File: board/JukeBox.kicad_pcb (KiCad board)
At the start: 2 copper layers, 78.5 x 80 mm, 44 parts, among them J1 USB_C_Receptacle_USB2.0, J2 Conn_01x02, J3 Conn_01x04, J4 Conn_01x03, SW1 SW_SPST, SW10 SW_SPST, SW11 SW_SPST, SW12 SW_SPST, SW2 SW_SPST, SW3 SW_SPST, SW4 SW_SPST, SW5 SW_SPST, SW6 SW_SPST, SW7 SW_SPST, SW8 SW_SPST, SW9 SW_SPST, U1 ATmega8U2-A, Y1 16MHz

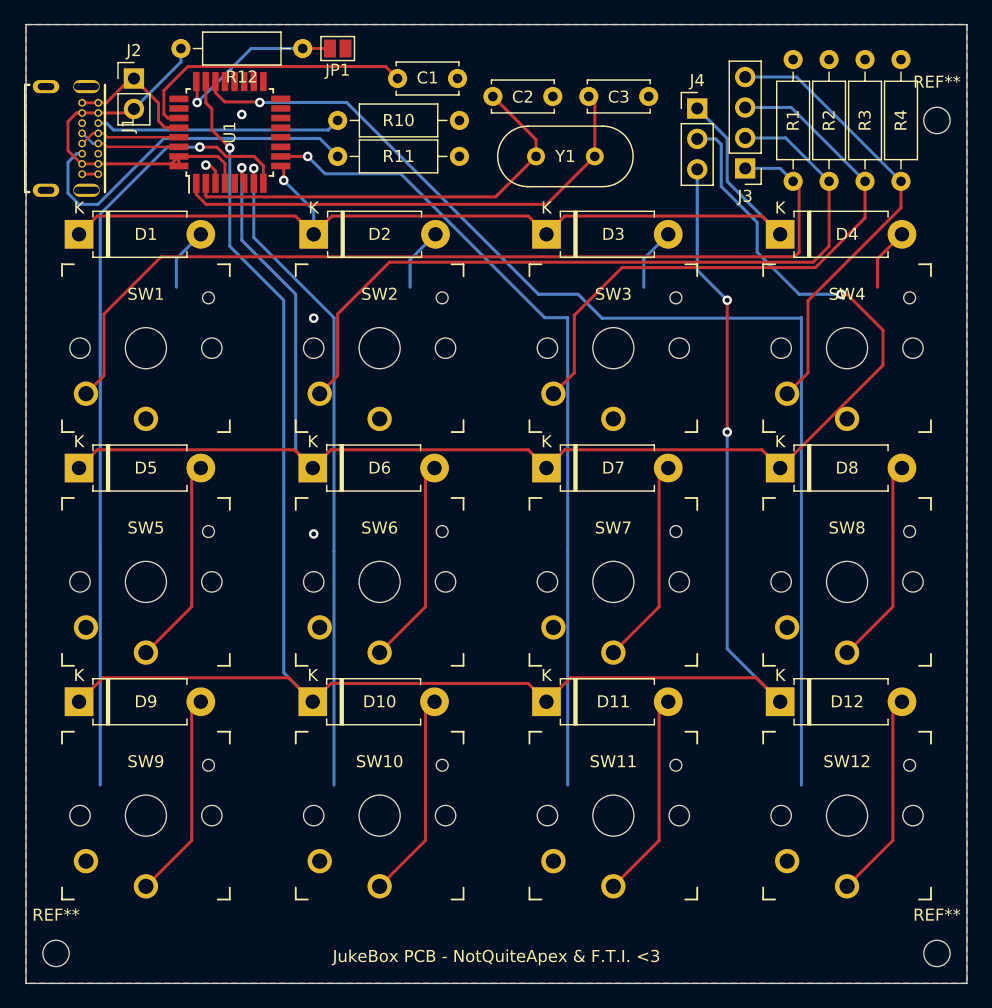
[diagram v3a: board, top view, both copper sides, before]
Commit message: update traces and usb c pads
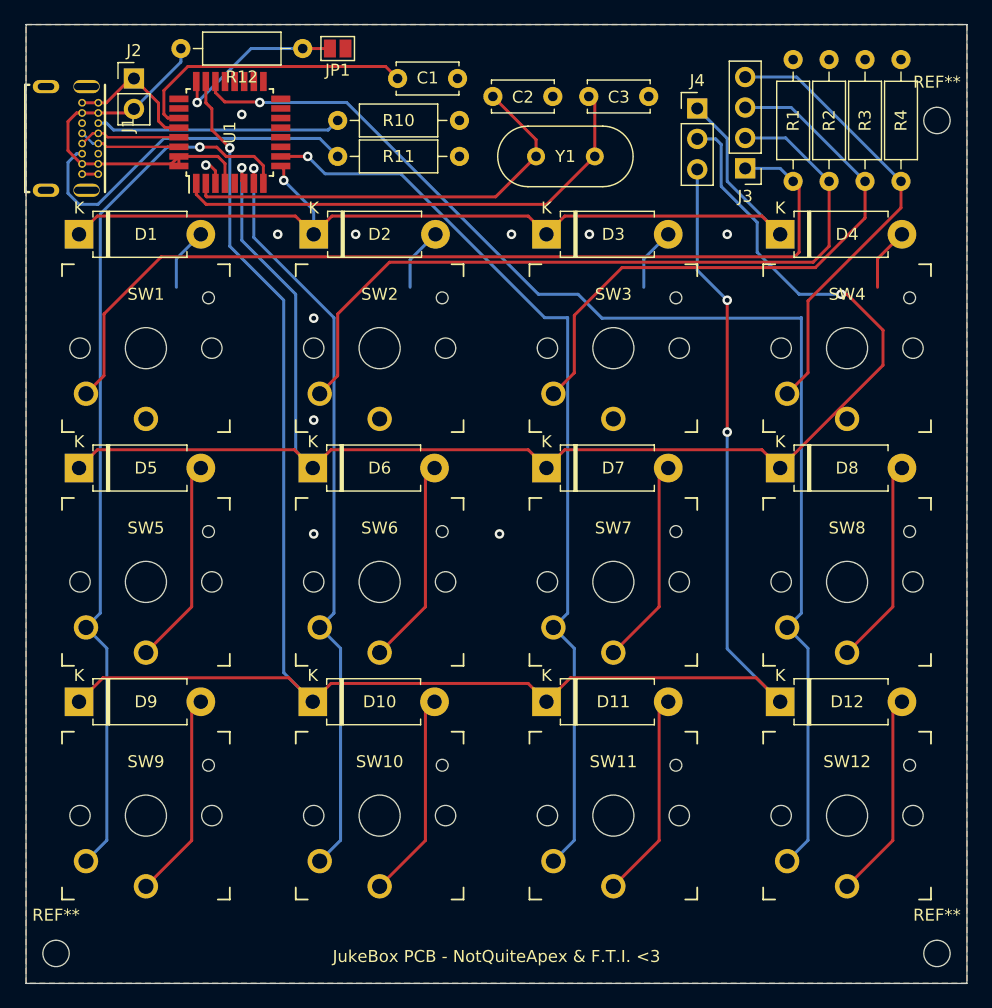
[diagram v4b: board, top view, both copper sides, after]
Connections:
- J1 pad P1: (no net) -> GND
- J1 pad P2: (no net) -> GND
- J1 pad P3: (no net) -> GND
- J1 pad P4: (no net) -> GND
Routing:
- net COL_4: track 134.9 -> 143.2 mm
- net COL_3: track 119.0 -> 127.3 mm
- net COL_1: track 143.7 -> 152.0 mm
- net COL_2: track 120.0 -> 128.3 mm
- net GND: vias 4 -> 11
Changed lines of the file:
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@@
     (pad "B12" thru_hole circle locked (at -2.975 -2.675 270) (size 0.65 0.65) (drill 0.4) (layers *.Cu *.Mask)
       (net 1 "GND") (pinfunction "GND") (pintype "passive"))
-    (pad "P1" thru_hole oval locked (at -4.325 -3.045 270) (size 1.108 2.216) (drill oval 0.6 2.1) (layers *.Cu *.Mask))
-    (pad "P2" thru_hole oval locked (at 4.325 -3.045 270) (size 1.108 2.216) (drill oval 0.6 2.1) (layers *.Cu *.Mask))
-    (pad "P3" thru_hole oval locked (at 4.325 0.335 270) (size 1.108 2.216) (drill oval 0.6 1.4) (layers *.Cu *.Mask))
-    (pad "P4" thru_hole oval locked (at -4.325 0.335 270) (size 1.108 2.216) (drill oval 0.6 1.4) (layers *.Cu *.Mask))
+    (pad "P1" thru_hole oval locked (at -4.325 -3.045 270) (size 1.108 2.216) (drill oval 0.6 2.1) (layers *.Cu *.Mask)
+      (net 1 "GND"))
+    (pad "P2" thru_hole oval locked (at 4.325 -3.045 270) (size 1.108 2.216) (drill oval 0.6 2.1) (layers *.Cu *.Mask)
+      (net 1 "GND"))
+    (pad "P3" thru_hole oval locked (at 4.325 0.335 270) (size 1.108 2.216) (drill oval 0.6 1.4) (layers *.Cu *.Mask)
+      (net 1 "GND"))
+    (pad "P4" thru_hole oval locked (at -4.325 0.335 270) (size 1.108 2.216) (drill oval 0.6 1.4) (layers *.Cu *.Mask)
+      (net 1 "GND"))
   )
   (footprint "Diode_THT:D_DO-15_P10.16mm_Horizontal" (layer "F.Cu")
@@
   (segment (start 113.025 47.475) (end 111.675 47.475) (width 0.25) (layer "F.Cu") (net 1))
   (segment (start 118.05 41.55) (end 118.05 43.05) (width 0.25) (layer "F.Cu") (net 1))
+  (via (at 131 68) (size 0.8) (drill 0.4) (layers "F.Cu" "B.Cu") (free) (net 1))
+  (via (at 134.5 52.5) (size 0.8) (drill 0.4) (layers "F.Cu" "B.Cu") (free) (net 1))
   (via (at 122 46.7245) (size 0.8) (drill 0.4) (layers "F.Cu" "B.Cu") (net 1))
+  (via (at 147.5 52.5) (size 0.8) (drill 0.4) (layers "F.Cu" "B.Cu") (free) (net 1))
+  (via (at 146.5 77.5) (size 0.8) (drill 0.4) (layers "F.Cu" "B.Cu") (free) (net 1))
   (via (at 131 59.5) (size 0.8) (drill 0.4) (layers "F.Cu" "B.Cu") (free) (net 1))
   (via (at 125 42.5) (size 0.8) (drill 0.4) (layers "F.Cu" "B.Cu") (free) (net 1))
+  (via (at 128 52.5) (size 0.8) (drill 0.4) (layers "F.Cu" "B.Cu") (free) (net 1))
+  (via (at 154 52.5) (size 0.8) (drill 0.4) (layers "F.Cu" "B.Cu") (free) (net 1))
   (via (at 131 77.5) (size 0.8) (drill 0.4) (layers "F.Cu" "B.Cu") (free) (net 1))
+  (via (at 165.5 52.5) (size 0.8) (drill 0.4) (layers "F.Cu" "B.Cu") (free) (net 1))
   (segment (start 118.825 42.8) (end 118.5 42.475) (width 0.25) (layer "F.Cu") (net 2))
   (segment (start 118.5 40.5) (end 120.5 38.5) (width 0.25) (layer "F.Cu") (net 2))
@@
   (via (at 121.5 45.2245) (size 0.8) (drill 0.4) (layers "F.Cu" "B.Cu") (net 28))
   (segment (start 167 47) (end 169.92 47) (width 0.25) (layer "B.Cu") (net 28))
-  (segment (start 113.19 98.46) (end 113.19 78.96) (width 0.25) (layer "B.Cu") (net 28))
-  (segment (start 113.19 50.81) (end 113.19 59.46) (width 0.25) (layer "B.Cu") (net 28))
+  (segment (start 112 85.3) (end 113.74147 87.04147) (width 0.25) (layer "B.Cu") (net 28))
+  (segment (start 113.19 50.81) (end 118.7755 45.2245) (width 0.25) (layer "B.Cu") (net 28))
+  (segment (start 112 85.3) (end 113.19 84.11) (width 0.25) (layer "B.Cu") (net 28))
   (segment (start 169.92 47) (end 171 48.08) (width 0.25) (layer "B.Cu") (net 28))
-  (segment (start 113.19 78.96) (end 113.19 59.46) (width 0.25) (layer "B.Cu") (net 28))
-  (segment (start 118.7755 45.2245) (end 113.19 50.81) (width 0.25) (layer "B.Cu") (net 28))
-  (segment (start 121.5 45.2245) (end 118.7755 45.2245) (width 0.25) (layer "B.Cu") (net 28))
+  (segment (start 113.74147 87.04147) (end 113.74147 103.05853) (width 0.25) (layer "B.Cu") (net 28))
+  (segment (start 118.7755 45.2245) (end 121.5 45.2245) (width 0.25) (layer "B.Cu") (net 28))
+  (segment (start 113.74147 103.05853) (end 112 104.8) (width 0.25) (layer "B.Cu") (net 28))
+  (segment (start 113.19 84.11) (end 113.19 50.81) (width 0.25) (layer "B.Cu") (net 28))
   (segment (start 133 64.3) (end 131.5 65.8) (width 0.25) (layer "F.Cu") (net 29))
   (segment (start 174 53.5) (end 172.67355 54.82645) (width 0.25) (layer "F.Cu") (net 29))
@@
   (segment (start 126 47) (end 126 48.25) (width 0.25) (layer "F.Cu") (net 29))
   (via (at 126 47) (size 0.8) (drill 0.4) (layers "F.Cu" "B.Cu") (net 29))
+  (segment (start 132.69 84.11) (end 131.5 85.3) (width 0.25) (layer "B.Cu") (net 29))
+  (segment (start 133.24147 87.04147) (end 133.24147 103.05853) (width 0.25) (layer "B.Cu") (net 29))
+  (segment (start 126 52.77) (end 132.69 59.46) (width 0.25) (layer "B.Cu") (net 29))
+  (segment (start 133.24147 103.05853) (end 131.5 104.8) (width 0.25) (layer "B.Cu") (net 29))
+  (segment (start 132.69 59.46) (end 132.69 84.11) (width 0.25) (layer "B.Cu") (net 29))
   (segment (start 167 44.46) (end 170.38 44.46) (width 0.25) (layer "B.Cu") (net 29))
-  (segment (start 126 52.77) (end 126 47) (width 0.25) (layer "B.Cu") (net 29))
-  (segment (start 132.69 59.46) (end 126 52.77) (width 0.25) (layer "B.Cu") (net 29))
-  (segment (start 132.69 59.46) (end 132.69 78.96) (width 0.25) (layer "B.Cu") (net 29))
+  (segment (start 126 47) (end 126 52.77) (width 0.25) (layer "B.Cu") (net 29))
+  (segment (start 131.5 85.3) (end 133.24147 87.04147) (width 0.25) (layer "B.Cu") (net 29))
   (segment (start 170.38 44.46) (end 174 48.08) (width 0.25) (layer "B.Cu") (net 29))
-  (segment (start 132.69 78.96) (end 132.69 98.46) (width 0.25) (layer "B.Cu") (net 29))
   (segment (start 177 51.136396) (end 172.859946 55.27645) (width 0.25) (layer "F.Cu") (net 30))
   (segment (start 156.72355 55.27645) (end 152.74147 59.25853) (width 0.25) (layer "F.Cu") (net 30))
@@
   (segment (start 177 48.08) (end 177 51.136396) (width 0.25) (layer "F.Cu") (net 30))
   (via (at 130.5 46) (size 0.8) (drill 0.4) (layers "F.Cu" "B.Cu") (net 30))
-  (segment (start 152.19 98.46) (end 152.19 78.96) (width 0.25) (layer "B.Cu") (net 30))
+  (segment (start 151 85.3) (end 152.19 84.11) (width 0.25) (layer "B.Cu") (net 30))
   (segment (start 170.84 41.92) (end 177 48.08) (width 0.25) (layer "B.Cu") (net 30))
   (segment (start 167 41.92) (end 170.84 41.92) (width 0.25) (layer "B.Cu") (net 30))
+  (segment (start 138.270277 47.453601) (end 131.953601 47.453601) (width 0.25) (layer "B.Cu") (net 30))
+  (segment (start 152.74147 103.05853) (end 151 104.8) (width 0.25) (layer "B.Cu") (net 30))
+  (segment (start 150.276676 59.46) (end 138.270277 47.453601) (width 0.25) (layer "B.Cu") (net 30))
+  (segment (start 131.953601 47.453601) (end 130.5 46) (width 0.25) (layer "B.Cu") (net 30))
+  (segment (start 152.19 84.11) (end 152.19 59.46) (width 0.25) (layer "B.Cu") (net 30))
   (segment (start 152.19 59.46) (end 150.276676 59.46) (width 0.25) (layer "B.Cu") (net 30))
-  (segment (start 152.19 78.96) (end 152.19 59.46) (width 0.25) (layer "B.Cu") (net 30))
-  (segment (start 138.270277 47.453601) (end 131.953601 47.453601) (width 0.25) (layer "B.Cu") (net 30))
-  (segment (start 131.953601 47.453601) (end 130.5 46) (width 0.25) (layer "B.Cu") (net 30))
-  (segment (start 150.276676 59.46) (end 138.270277 47.453601) (width 0.25) (layer "B.Cu") (net 30))
+  (segment (start 152.74147 87.04147) (end 152.74147 103.05853) (width 0.25) (layer "B.Cu") (net 30))
+  (segment (start 151 85.3) (end 152.74147 87.04147) (width 0.25) (layer "B.Cu") (net 30))
   (segment (start 172.24147 58.04853) (end 172.24147 64.05853) (width 0.25) (layer "F.Cu") (net 31))
   (segment (start 180 50.29) (end 172.24147 58.04853) (width 0.25) (layer "F.Cu") (net 31))
@@
   (segment (start 126.5 41.5) (end 126.456895 41.456895) (width 0.25) (layer "F.Cu") (net 31))
   (via (at 126.5 41.5) (size 0.8) (drill 0.4) (layers "F.Cu" "B.Cu") (net 31))
+  (segment (start 170.5 85.3) (end 172.24147 87.04147) (width 0.25) (layer "B.Cu") (net 31))
   (segment (start 167 39.38) (end 171.3 39.38) (width 0.25) (layer "B.Cu") (net 31))
   (segment (start 153.052373 57.5) (end 155.052373 59.5) (width 0.25) (layer "B.Cu") (net 31))
-  (segment (start 171.69 59.46) (end 171.69 78.96) (width 0.25) (layer "B.Cu") (net 31))
-  (segment (start 155.052373 59.5) (end 171.65 59.5) (width 0.25) (layer "B.Cu") (net 31))
-  (segment (start 171.69 78.96) (end 171.69 98.46) (width 0.25) (layer "B.Cu") (net 31))
-  (segment (start 171.65 59.5) (end 171.69 59.46) (width 0.25) (layer "B.Cu") (net 31))
   (segment (start 133.748602 41.5) (end 149.748602 57.5) (width 0.25) (layer "B.Cu") (net 31))
-  (segment (start 171.3 39.38) (end 180 48.08) (width 0.25) (layer "B.Cu") (net 31))
+  (segment (start 172.24147 87.04147) (end 172.24147 103.05853) (width 0.25) (layer "B.Cu") (net 31))
   (segment (start 126.5 41.5) (end 133.748602 41.5) (width 0.25) (layer "B.Cu") (net 31))
   (segment (start 149.748602 57.5) (end 153.052373 57.5) (width 0.25) (layer "B.Cu") (net 31))
+  (segment (start 171.3 39.38) (end 180 48.08) (width 0.25) (layer "B.Cu") (net 31))
+  (segment (start 171.69 84.11) (end 170.5 85.3) (width 0.25) (layer "B.Cu") (net 31))
+  (segment (start 172.24147 103.05853) (end 170.5 104.8) (width 0.25) (layer "B.Cu") (net 31))
+  (segment (start 171.65 59.5) (end 171.69 59.46) (width 0.25) (layer "B.Cu") (net 31))
+  (segment (start 171.69 59.46) (end 171.69 84.11) (width 0.25) (layer "B.Cu") (net 31))
+  (segment (start 155.052373 59.5) (end 171.65 59.5) (width 0.25) (layer "B.Cu") (net 31))
   (zone (net 1) (net_name "GND") (layer "F.Cu") (hatch edge 0.508)
     (connect_pads (clearance 0.508))

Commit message: fix some traces that werent connected properly
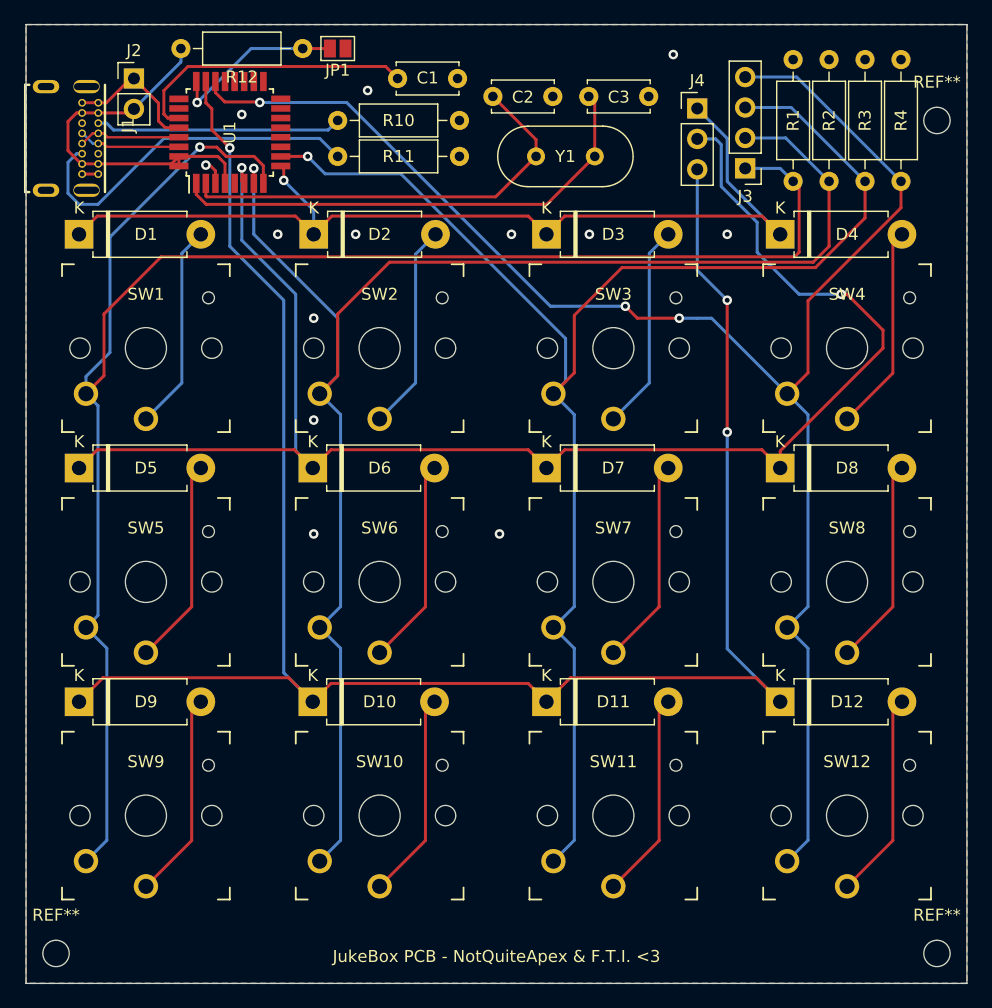
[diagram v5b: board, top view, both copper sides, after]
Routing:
- net Net-(D1-Pad2): track 5.26 -> 17.3 mm
- net Net-(D3-Pad2): track 5.26 -> 17.3 mm
- net Net-(D2-Pad2): track 5.30 -> 17.3 mm
- net Net-(D4-Pad2): track 5.26 -> 17.3 mm
- net COL_4: track 143.2 -> 139.2 mm, vias 1 -> 3
- net COL_2: track 128.3 -> 130.0 mm
- net COL_1: track 152.0 -> 151.2 mm
- net GND: vias 11 -> 13

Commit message: fast forward
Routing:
- net GND: vias 13 -> 14
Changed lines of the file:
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@@
   (via (at 154 52.5) (size 0.8) (drill 0.4) (layers "F.Cu" "B.Cu") (free) (net 1))
   (via (at 131 77.5) (size 0.8) (drill 0.4) (layers "F.Cu" "B.Cu") (free) (net 1))
+  (via (at 119.5 49.5) (size 0.8) (drill 0.4) (layers "F.Cu" "B.Cu") (free) (net 1))
   (via (at 165.5 52.5) (size 0.8) (drill 0.4) (layers "F.Cu" "B.Cu") (free) (net 1))
   (segment (start 118.825 42.8) (end 118.5 42.475) (width 0.25) (layer "F.Cu") (net 2))

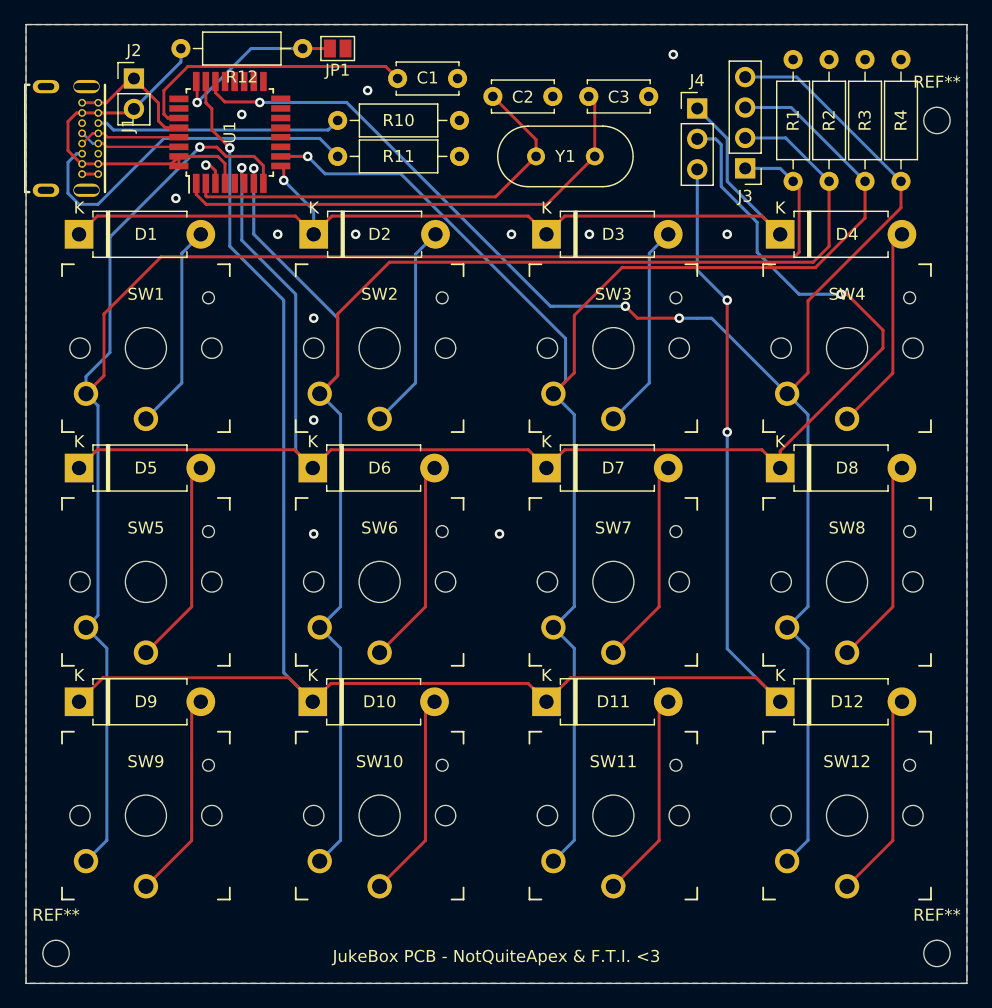
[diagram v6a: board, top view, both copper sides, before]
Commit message: mix cherry mx and kailh footprints1
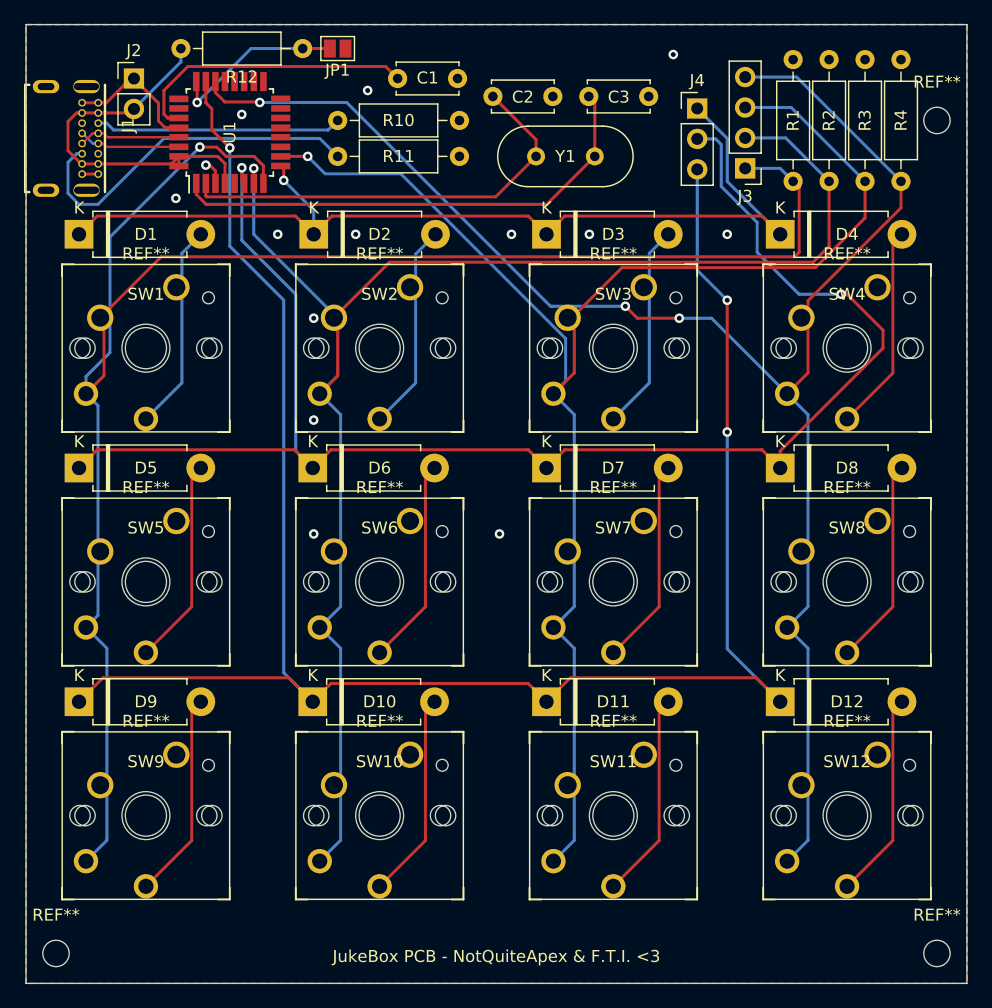
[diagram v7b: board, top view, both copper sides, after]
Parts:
- added REF**: SW_Cherry_MX_1.00u_PCB, Button_Switch_Keyboard:SW_Cherry_MX_1.00u_PCB, F.Cu at (158.5, 76.4)
- added REF**: SW_Cherry_MX_1.00u_PCB, Button_Switch_Keyboard:SW_Cherry_MX_1.00u_PCB, F.Cu at (119.5, 76.4)
- added REF**: SW_Cherry_MX_1.00u_PCB, Button_Switch_Keyboard:SW_Cherry_MX_1.00u_PCB, F.Cu at (139.0, 95.9)
- added REF**: SW_Cherry_MX_1.00u_PCB, Button_Switch_Keyboard:SW_Cherry_MX_1.00u_PCB, F.Cu at (119.5, 95.9)
- added REF**: SW_Cherry_MX_1.00u_PCB, Button_Switch_Keyboard:SW_Cherry_MX_1.00u_PCB, F.Cu at (139.0, 56.9)
- added REF**: SW_Cherry_MX_1.00u_PCB, Button_Switch_Keyboard:SW_Cherry_MX_1.00u_PCB, F.Cu at (158.5, 95.9)
- added REF**: SW_Cherry_MX_1.00u_PCB, Button_Switch_Keyboard:SW_Cherry_MX_1.00u_PCB, F.Cu at (178.0, 95.9)
- added REF**: SW_Cherry_MX_1.00u_PCB, Button_Switch_Keyboard:SW_Cherry_MX_1.00u_PCB, F.Cu at (119.5, 56.9)
- added REF**: SW_Cherry_MX_1.00u_PCB, Button_Switch_Keyboard:SW_Cherry_MX_1.00u_PCB, F.Cu at (139.0, 76.4)
- added REF**: SW_Cherry_MX_1.00u_PCB, Button_Switch_Keyboard:SW_Cherry_MX_1.00u_PCB, F.Cu at (158.5, 56.9)
- added REF**: SW_Cherry_MX_1.00u_PCB, Button_Switch_Keyboard:SW_Cherry_MX_1.00u_PCB, F.Cu at (178.0, 76.4)
- added REF**: SW_Cherry_MX_1.00u_PCB, Button_Switch_Keyboard:SW_Cherry_MX_1.00u_PCB, F.Cu at (178.0, 56.9)
